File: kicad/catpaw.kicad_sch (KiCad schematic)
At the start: 38 parts, among them J1 Conn_01x01_Socket_red, J2 Conn_01x01_Socket_black, J3 m12,Acode,5pin,femalesocket (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, J4 m8, 4Pin Supply Connector FEM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, J5 m8, 4Pin Supply Connector Bec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, J6 m12,Acode,5pin,femalesocket B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, J7 m12,Acode,5pin,femalesocket C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, SW1 SW_DPST, U1 INA826, U3 LM1458mx

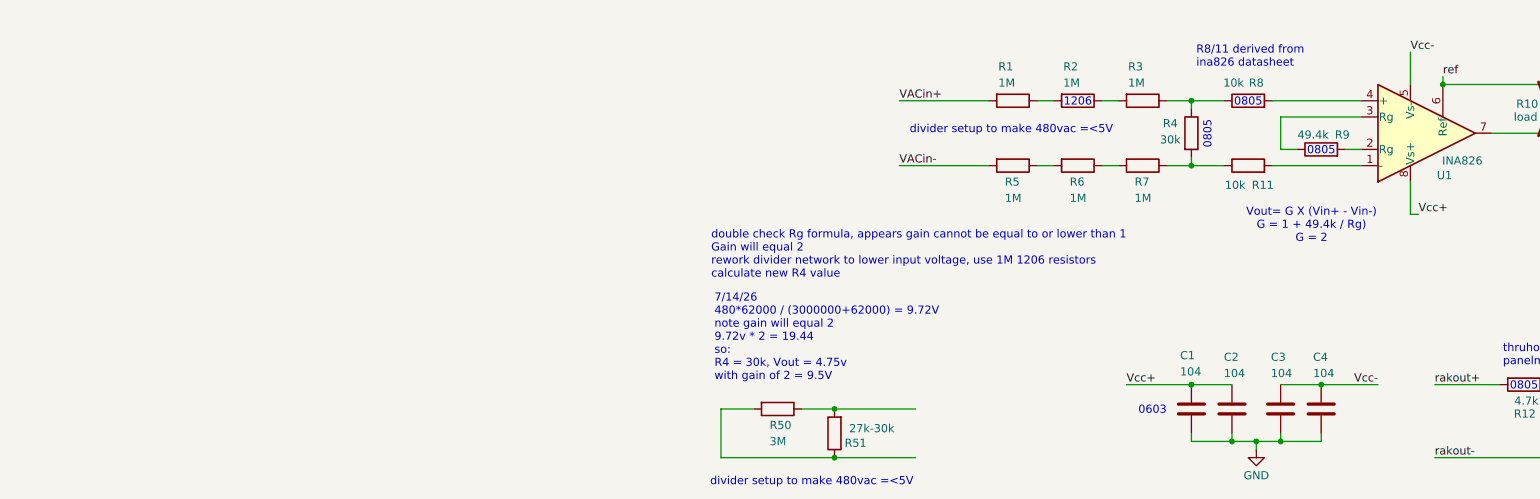
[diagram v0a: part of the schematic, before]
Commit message: Reorganized file structure
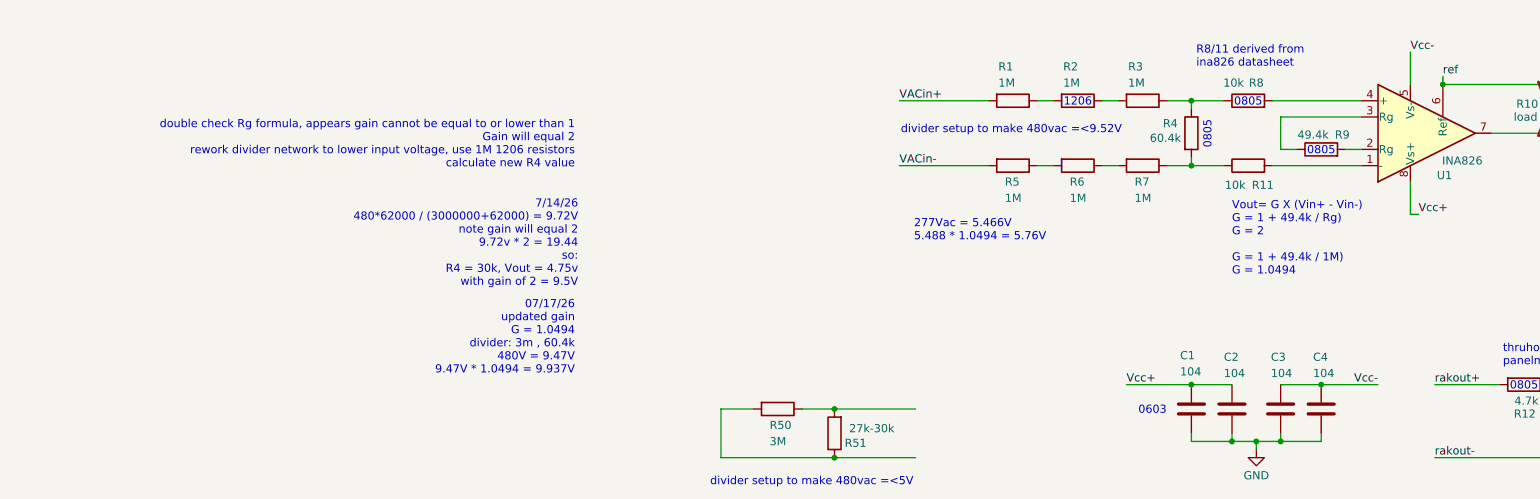
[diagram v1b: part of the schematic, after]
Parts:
- R4: value 30k -> 60.4k
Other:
- note added: "07/17/26 updated gain G = 1.0494 divider: 3m , 60.4k 480V = 9.47V 9.47V * 1.0494 = 9.937V"
- note added: "277Vac = 5.466V 5.488 * 1.0494 = 5.76V"
- note added: "Vout= G X (Vin+ - Vin-) G = 1 + 49.4k / Rg) G = 2 G = 1 + 49.4k / 1M) G = 1.0494"
- note added: "divider setup to make 480vac =<9.52V"
- note removed: "Vout= G X (Vin+ - Vin-) G = 1 + 49.4k / Rg) G = 2"
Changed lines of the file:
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@@
 		)
 	)
-	(text "divider setup to make 480vac =<5V"
+	(text "divider setup to make 480vac =<9.52V"
 		(exclude_from_sim no)
 		(at 65.786 136.652 0)
@@
 	(text "7/14/26\n480*62000 / (3000000+62000) = 9.72V \nnote gain will equal 2\n9.72v * 2 = 19.44\nso:\nR4 = 30k, Vout = 4.75v\nwith gain of 2 = 9.5V"
 		(exclude_from_sim no)
-		(at 19.304 169.164 0)
+		(at -2.032 154.432 0)
 		(effects
 			(font
 				(size 1.27 1.27)
 			)
-			(justify left)
+			(justify right)
 		)
 	)
@@
 		)
 	)
+	(text "277Vac = 5.466V\n5.488 * 1.0494 = 5.76V"
+		(exclude_from_sim no)
+		(at 50.546 152.4 0)
+		(effects
+			(font
+				(size 1.27 1.27)
+			)
+			(justify left)
+		)
+	)
 	(text "m8 Up+- & m12 Up+- \nare connected in beckhoff"
 		(exclude_from_sim no)
@@
 	(text "double check Rg formula, appears gain cannot be equal to or lower than 1\nGain will equal 2\nrework divider network to lower input voltage, use 1M 1206 resistors\ncalculate new R4 value\n"
 		(exclude_from_sim no)
-		(at 18.796 156.21 0)
+		(at -2.54 138.938 0)
 		(effects
 			(font
 				(size 1.27 1.27)
 			)
-			(justify left)
+			(justify right)
 		)
 	)
@@
 		)
 	)
+	(text "07/17/26\nupdated gain\nG = 1.0494\ndivider: 3m , 60.4k\n480V = 9.47V\n9.47V * 1.0494 = 9.937V"
+		(exclude_from_sim no)
+		(at -2.54 169.164 0)
+		(effects
+			(font
+				(size 1.27 1.27)
+			)
+			(justify right)
+		)
+	)
 	(text "thruhole LED\npanelmount"
 		(exclude_from_sim no)
@@
 		)
 	)
-	(text "Vout= G X (Vin+ - Vin-)\nG = 1 + 49.4k / Rg)\nG = 2"
+	(text "Vout= G X (Vin+ - Vin-)\nG = 1 + 49.4k / Rg)\nG = 2\n\nG = 1 + 49.4k / 1M)\nG = 1.0494"
 		(exclude_from_sim no)
-		(at 112.776 151.638 0)
+		(at 100.33 153.67 0)
 		(effects
 			(font
 				(size 1.27 1.27)
 			)
+			(justify left)
 		)
 	)
@@
 			)
 		)
-		(property "Value" "30k"
-			(at 90.678 138.176 0)
+		(property "Value" "60.4k"
+			(at 89.916 137.922 0)
 			(effects
 				(font

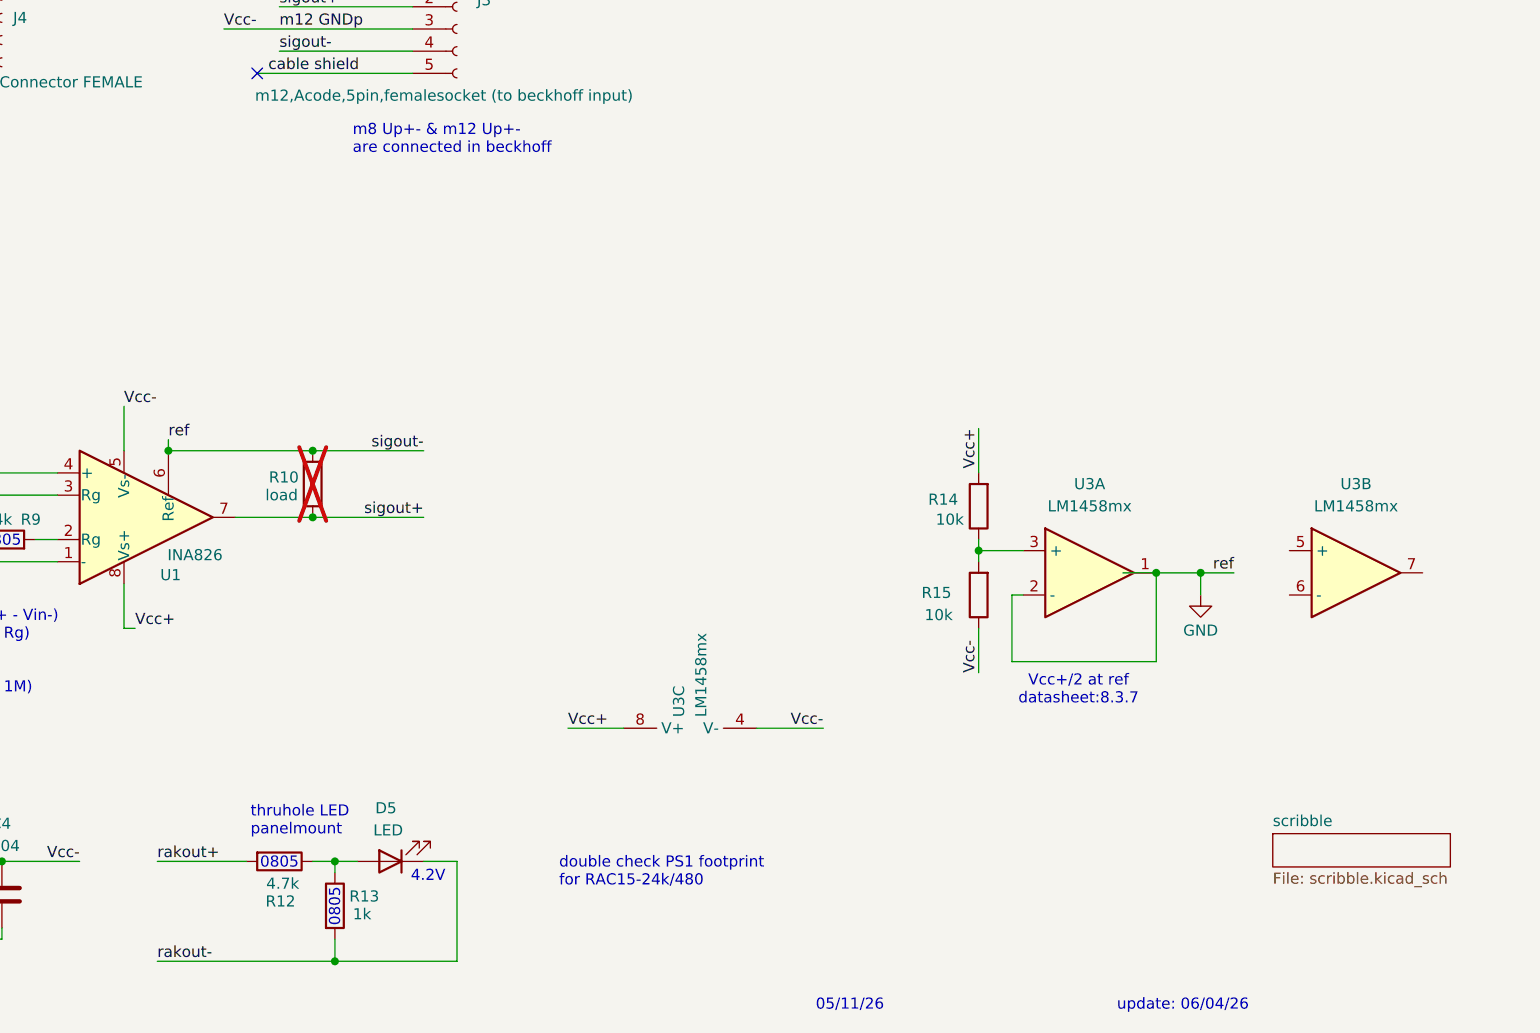
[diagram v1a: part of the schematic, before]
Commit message: Footprints assigned
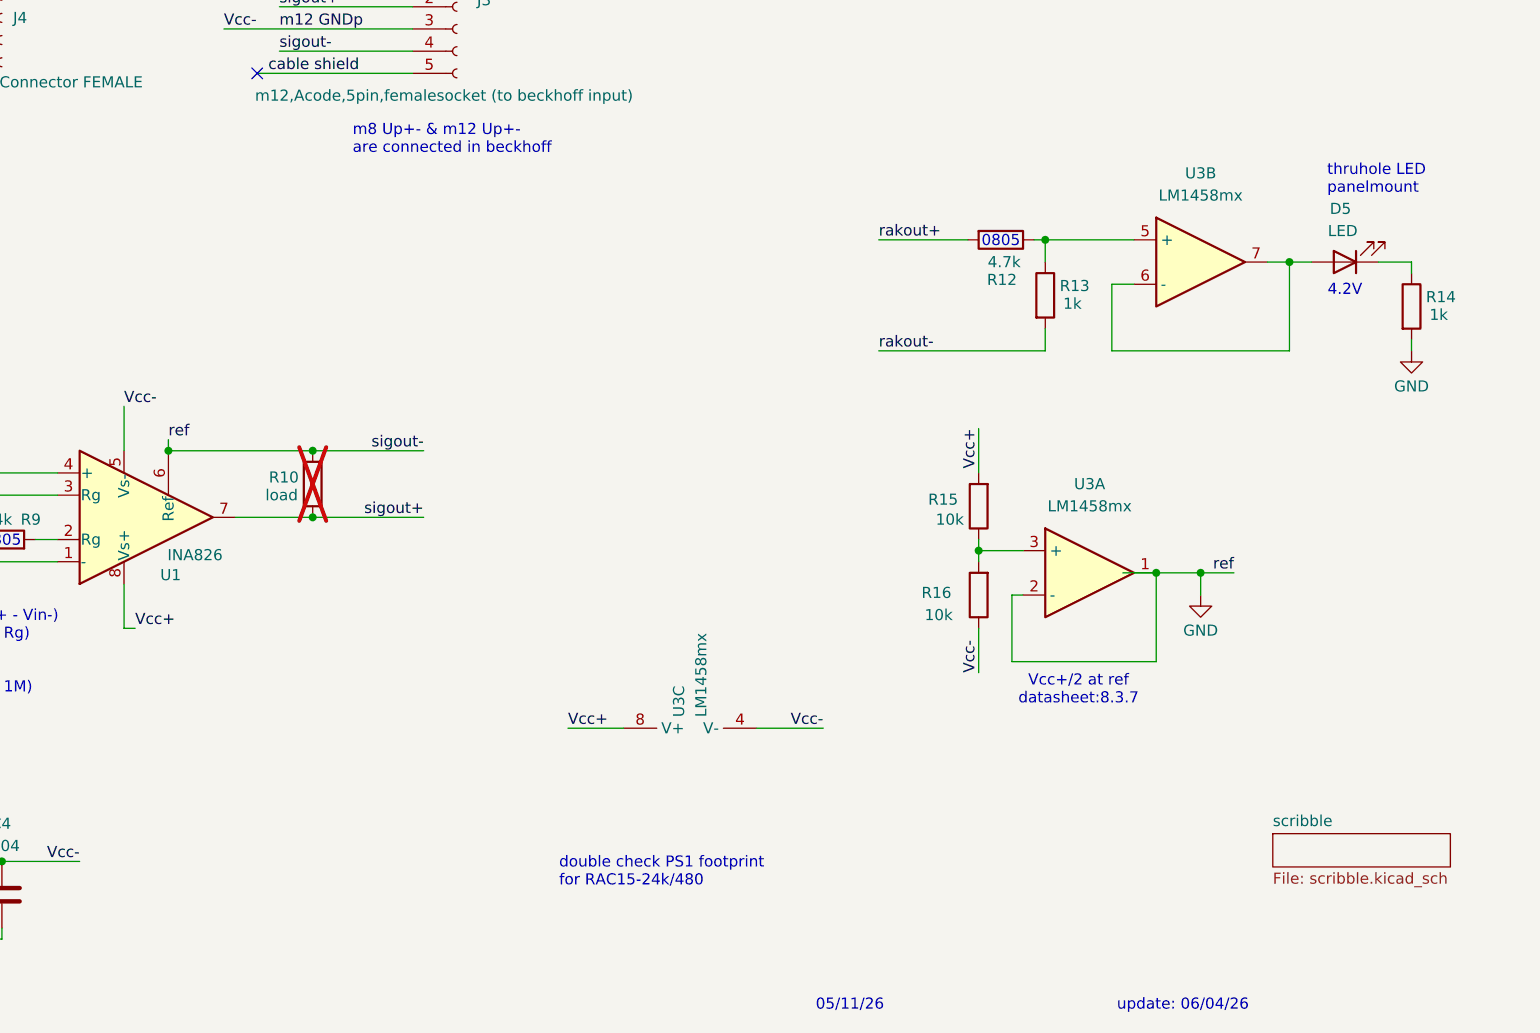
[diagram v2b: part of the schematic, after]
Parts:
- added R14: 1k, Resistor_SMD:R_0805_2012Metric_Pad1.20x1.40mm_HandSolder, symbol Device:R
- C1, C2, C3, C4: footprint 0603 -> Capacitor_SMD:C_0603_1608Metric_Pad1.08x0.95mm_HandSolder
- D5: footprint (none) -> Diode_THT:D_5W_P5.08mm_Vertical_AnodeUp
- F1: footprint (none) -> kyuditsky_kicad:FUSC10131X312N
- J1, J2: footprint (none) -> kyuditsky_kicad:Banana_Jack_S_RA_73099
- J3: footprint (none) -> kyuditsky_kicad:M12A05PFFRSF7003
- J4: footprint (none) -> kyuditsky_kicad:CDM84504AFPF01067
- R1, R2, R3, R5, R6, R7: footprint (none) -> Resistor_SMD:R_1206_3216Metric_Pad1.30x1.75mm_HandSolder
- R10, R11, R12, R13, R4, R8, R9: footprint (none) -> Resistor_SMD:R_0805_2012Metric_Pad1.20x1.40mm_HandSolder
- R15: renamed from R14; footprint (none) -> Resistor_SMD:R_0805_2012Metric_Pad1.20x1.40mm_HandSolder
- R16: renamed from R15; footprint (none) -> Resistor_SMD:R_0805_2012Metric_Pad1.20x1.40mm_HandSolder
- SW1: footprint (none) -> kyuditsky_kicad:switch - 1MD1T1B1M6QES
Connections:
- net GND: now also R14.2
- net rakout-: no longer D5.1 (K)
- net at R12.1, R13.1: now also U3.5 (+); no longer D5.2 (A)
- net at U3.6 (-): now also D5.2 (A), U3.7
- new net: D5.1 (K), R14.1
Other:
- moved on the sheet: D5, R12, R13, U3B

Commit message: added scheme screenshot
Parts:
- R9: value 49.4k -> 1M
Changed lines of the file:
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@@
 			)
 		)
-		(property "Value" "49.4k"
+		(property "Value" "1M"
 			(at 113.03 137.414 90)
 			(effects

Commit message: began pcbnew layout
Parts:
- removed SW1: SW_DPST, kyuditsky_kicad:switch - 1MD1T1B1M6QES, symbol Switch:SW_DPST
- added SW1: 1MD1T1B1M6QES, kyuditsky_kicad:switch - 1MD1T1B1M6QES, symbol Switch:SW_Push_DPDT
- renumbered U3 to U2
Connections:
- net VACin+: now also SW1.2 (B)
- net VACin-: now also SW1.5 (B)
- net at PS1.1 (AC(N)): now also SW1.4 (A)
- net at F1.1: now also SW1.1 (A)
- no-connect marks 3 -> 5
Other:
- note added: "update: 07/20/26"
- note removed: "update: 06/04/26"
- moved on the sheet: C1, C2, C3, C4, D1, D2, D3, D4, D5, F1, J1, J2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

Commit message: pcbnew initial route
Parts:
- renumbered C3 to C2, C2 to C3, R9 to R10, R10 to R11, R5 to R4, R6 to R5, R7 to R6, R4 to R7, R11 to R9
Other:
- note added: "note multiple names for gnd"
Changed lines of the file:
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@@
 		)
 	)
+	(text "note multiple names for gnd"
+		(exclude_from_sim no)
+		(at 160.02 177.8 0)
+		(effects
+			(font
+				(size 1.27 1.27)
+			)
+		)
+	)
 	(text "480v clearance = 8mm"
 		(exclude_from_sim no)
@@
 	)
 	(junction
+		(at 165.1 166.37)
+		(diameter 0)
+		(color 0 0 0 0)
+	)
+	(junction
 		(at 44.45 52.07)
 		(diameter 0)
@@
 	(wire
 		(pts
+			(xy 165.1 162.56) (xy 165.1 166.37)
+		)
+		(stroke
+			(width 0)
+			(type default)
+		)
+	)
+	(wire
+		(pts
 			(xy 86.36 113.03) (xy 88.9 113.03)
 		)
@@
 	(wire
 		(pts
+			(xy 157.48 166.37) (xy 165.1 166.37)
+		)
+		(stroke
+			(width 0)
+			(type default)
+		)
+	)
+	(wire
+		(pts
 			(xy 96.52 90.17) (xy 107.95 90.17)
 		)
@@
 	(wire
 		(pts
+			(xy 157.48 162.56) (xy 165.1 162.56)
+		)
+		(stroke
+			(width 0)
+			(type default)
+		)
+	)
+	(wire
+		(pts
 			(xy 48.26 118.11) (xy 53.34 118.11)
 		)
@@
 	(wire
 		(pts
+			(xy 165.1 170.18) (xy 165.1 166.37)
+		)
+		(stroke
+			(width 0)
+			(type default)
+		)
+	)
+	(wire
+		(pts
 			(xy -34.29 186.69) (xy -16.51 186.69)
 		)
@@
 		)
 	)
+	(label "ref"
+		(at 157.48 166.37 0)
+		(effects
+			(font
+				(size 1.27 1.27)
+			)
+			(justify left bottom)
+		)
+	)
 	(label "sigout-"
 		(at 144.78 88.9 0)
@@
 		)
 	)
+	(label "sigout-"
+		(at 157.48 162.56 0)
+		(effects
+			(font
+				(size 1.27 1.27)
+			)
+			(justify left bottom)
+		)
+	)
 	(label "Up Peripheral V"
 		(at 22.86 29.21 0)
@@
 		(on_board yes)
 		(dnp no)
-		(property "Reference" "R5"
+		(property "Reference" "R4"
 			(at 64.77 144.7799 90)
 			(effects
@@
 			(project "may"
 				(path "/c6afa226-7a71-49a1-9fd2-6abf112b3631"
-					(reference "R5")
+					(reference "R4")
 					(unit 1)
 				)
@@
 		(on_board yes)
 		(dnp no)
-		(property "Reference" "C2"
+		(property "Reference" "C3"
 			(at 250.19 135.382 0)
 			(effects
@@
 			(project "may"
 				(path "/c6afa226-7a71-49a1-9fd2-6abf112b3631"
-					(reference "C2")
+					(reference "C3")
 					(unit 1)
 				)
@@
 		(on_board yes)
 		(dnp no)
-		(property "Reference" "C3"
+		(property "Reference" "C2"
 			(at 257.556 135.382 0)
 			(effects
@@
 			(project "catpaw"
 				(path "/c6afa226-7a71-49a1-9fd2-6abf112b3631"
-					(reference "C3")
+					(reference "C2")
 					(unit 1)
 				)
@@
 		(on_board yes)
 		(dnp no)
-		(property "Reference" "R9"
+		(property "Reference" "R10"
 			(at 117.602 137.414 90)
 			(effects
@@
 			(project "may"
 				(path "/c6afa226-7a71-49a1-9fd2-6abf112b3631"
-					(reference "R9")
+					(reference "R10")
 					(unit 1)
 				)
@@
 		(on_board yes)
 		(dnp no)
-		(property "Reference" "R11"
+		(property "Reference" "R9"
 			(at 105.156 145.288 90)
 			(effects
@@
 			(project "may"
 				(path "/c6afa226-7a71-49a1-9fd2-6abf112b3631"
-					(reference "R11")
+					(reference "R9")
 					(unit 1)
 				)
@@
 		(on_board yes)
 		(dnp no)
-		(property "Reference" "R6"
+		(property "Reference" "R5"
 			(at 74.93 144.7799 90)
 			(effects
@@
 			(project "may"
 				(path "/c6afa226-7a71-49a1-9fd2-6abf112b3631"
-					(reference "R6")
+					(reference "R5")
 					(unit 1)
 				)
@@
 		(on_board yes)
 		(dnp no)
-		(property "Reference" "R7"
+		(property "Reference" "R6"
 			(at 85.09 144.7799 90)
 			(effects
@@
 			(project "may"
 				(path "/c6afa226-7a71-49a1-9fd2-6abf112b3631"
-					(reference "R7")
+					(reference "R6")
 					(unit 1)
 				)
@@
 		(on_board yes)
 		(dnp no)
-		(property "Reference" "R4"
+		(property "Reference" "R7"
 			(at 90.678 135.636 0)
 			(effects
@@
 			(project "may"
 				(path "/c6afa226-7a71-49a1-9fd2-6abf112b3631"
-					(reference "R4")
+					(reference "R7")
 					(unit 1)
 				)
@@
 		(on_board yes)
 		(dnp yes)
-		(property "Reference" "R10"
+		(property "Reference" "R11"
 			(at 146.558 132.588 0)
 			(effects
@@
 			(project "may"
 				(path "/c6afa226-7a71-49a1-9fd2-6abf112b3631"
-					(reference "R10")
+					(reference "R11")
 					(unit 1)
 				)
@@
 					(unit 1)
 				)
+			)
+		)
+	)
+	(symbol
+		(lib_id "power:GND")
+		(at 165.1 170.18 0)
+		(unit 1)
+		(exclude_from_sim no)
+		(in_bom yes)
+		(on_board yes)
+		(dnp no)
+		(property "Reference" "#PWR04"
+			(at 165.1 176.53 0)
+			(effects
+				(font
+					(size 1.27 1.27)
+				)
+				(hide yes)
+			)
+		)
+		(property "Value" "GND"
+			(at 165.1 174.244 0)
+			(effects
+				(font
+					(size 1.27 1.27)
+				)
+			)
+		)
+		(property "Footprint" ""
+			(at 165.1 170.18 0)
+			(effects
+				(font
+					(size 1.27 1.27)
+				)
+				(hide yes)
+			)
+		)
+		(property "Datasheet" ""
+			(at 165.1 170.18 0)
+			(effects
+				(font
+					(size 1.27 1.27)
+				)
+				(hide yes)
+			)
+		)
+		(property "Description" "Power symbol creates a global label with name \"GND\" , ground"
+			(at 165.1 170.18 0)
+			(effects
+				(font
+					(size 1.27 1.27)
+				)
+				(hide yes)
+			)
+		)
+		(pin "1"
+		)
+		(instances
+			(project "catpaw"
+				(path "/c6afa226-7a71-49a1-9fd2-6abf112b3631"
+					(reference "#PWR04")
+					(unit 1)
+				)

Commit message: Exported BOM01, notes to scheme, touched up pcbnew
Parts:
- removed D3, D4: 1N5819, Diode_THT:D_DO-41_SOD81_P10.16mm_Horizontal, symbol Diode:1N5819
- D5: footprint Diode_THT:D_5W_P5.08mm_Vertical_AnodeUp -> LED_THT:LED_D5.0mm_Horizontal_O1.27mm_Z3.0mm
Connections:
- net m8 GNDs is gone; now on net m8 GNDp: J4.3 (Pin_3)
- net rakout- is gone; now on net m8 GNDp: PS1.4 (-Vout), R13.2
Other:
- note added: "R8/R9 derived from ina826 datasheet"
- note added: "consider capacitor across Sig+ / Sig- if interferance issues"
- note added: "double check diode polarity on negative side *removed gnd side diodes note, m8,m12 are physically unable to be inserted incorrectly"
- note added: "note multiple names for gnd note rakout- will be connected to gndp, gnds in turn connected to Vcc- m12 GNDp in the beckhoff which should be fine *is intentional"
- note added: "tvs or zener overvoltage protection?"
- note removed: "R8/11 derived from ina826 datasheet"
- note removed: "for 7/15/26: m8, m12 connectors & footprints switch footprint ina825 footprint base pcbnew layout determine approx case dimensions based on footprints/connectors"
- note removed: "note multiple names for gnd"
- moved on the sheet: F1, PS1, R1, R10, R11, R2, R3, R4, R5, R6, R7, R8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

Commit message: added test points and jumpers
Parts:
- added J8: Conn_01x01_Pin, Connector_PinHeader_2.54mm:PinHeader_1x01_P2.54mm_Vertical, symbol Connector:Conn_01x01_Pin
- added R17, R20: 0, Resistor_SMD:R_0805_2012Metric_Pad1.20x1.40mm_HandSolder, symbol Device:R
- added R18, R19: 0, Resistor_THT:R_Axial_DIN0204_L3.6mm_D1.6mm_P2.54mm_Vertical, symbol Device:R
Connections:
- net GND: now also J8.1 (Pin_1)
- net Vcc+: now also R17.2, R18.2
- net Vcc-: now also R19.2, R20.2
- net m8 GNDp: now also R19.1, R20.1
- net m8 Up: now also R17.1, R18.1

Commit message: updated bode plots, noted schematic
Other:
- note added: "RAC15-24sk/480 has a larger footprint than called for. Substituting RAC10-24SK/277 instead."
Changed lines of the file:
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@@
+		)
+	)
+	(text "RAC15-24sk/480 has a larger footprint than called for. \nSubstituting RAC10-24SK/277 instead."
+		(exclude_from_sim no)
+		(at 109.728 115.316 0)
+		(effects
+			(font
+				(size 1.27 1.27)
+			)
+			(justify left)
 		)
 	)
